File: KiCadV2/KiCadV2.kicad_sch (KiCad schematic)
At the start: 52 parts, among them J1 USB_C_Receptacle_PowerOnly_6P, J3 Screw_Terminal_01x02, J4 Screw_Terminal_01x02, U1 MT3608, U14 74LV08AT14-13, U16 NC7SZ157P6X, U17 MX3502S, U18 MX3502S, U2 74HC595, U26 MX3502S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

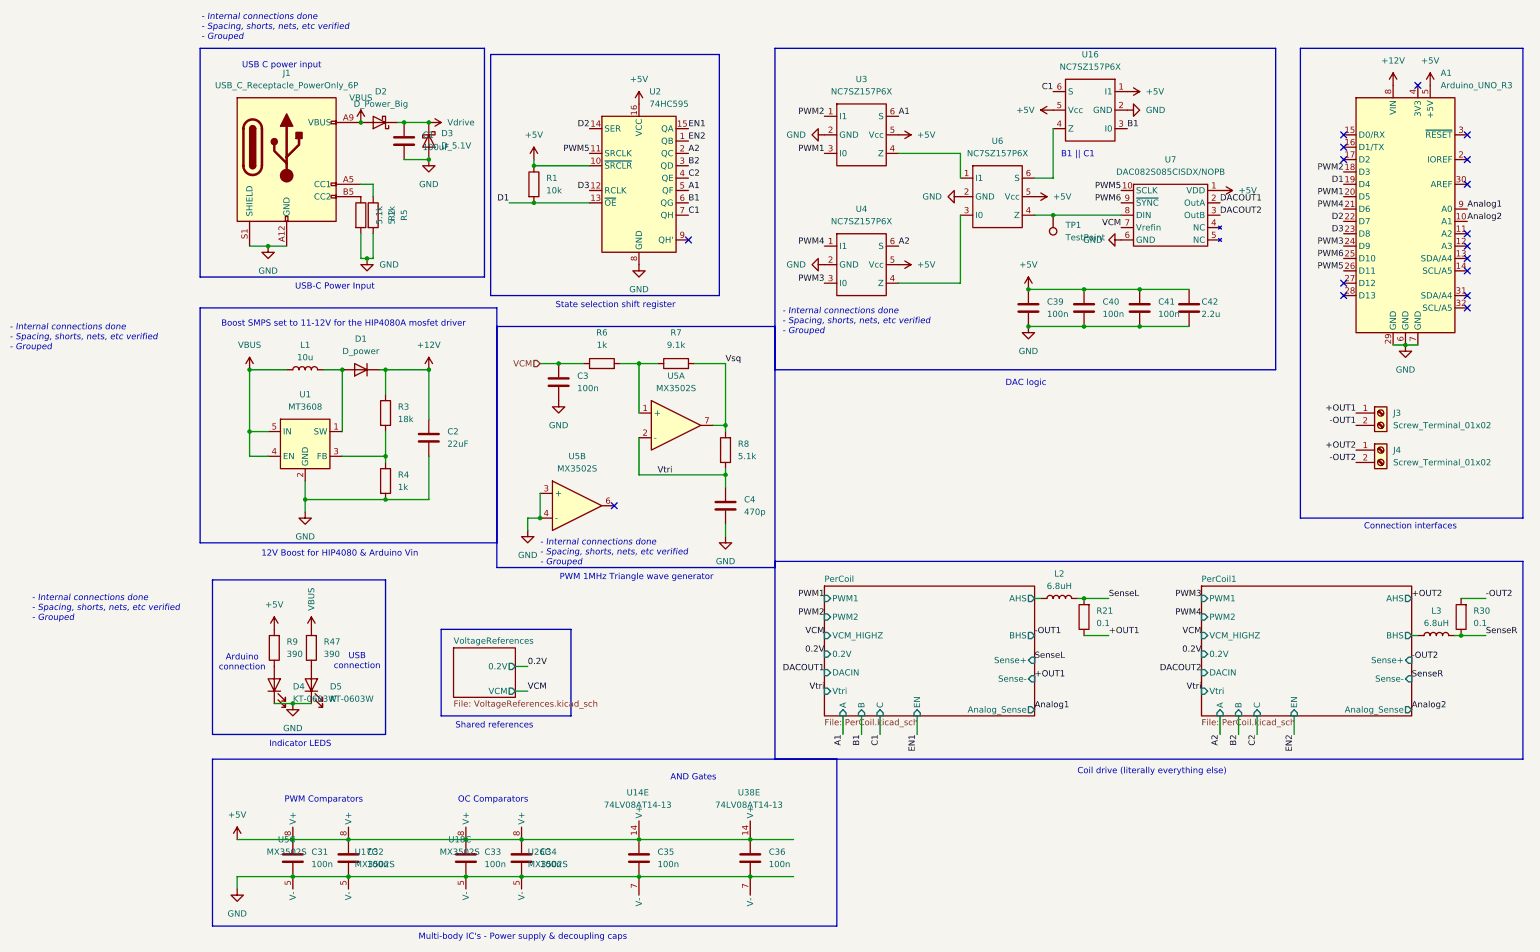
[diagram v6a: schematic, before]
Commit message: Fixed AND Gate pins, added extra DAC logic Mux
DAC logic mux not yet done on PCB
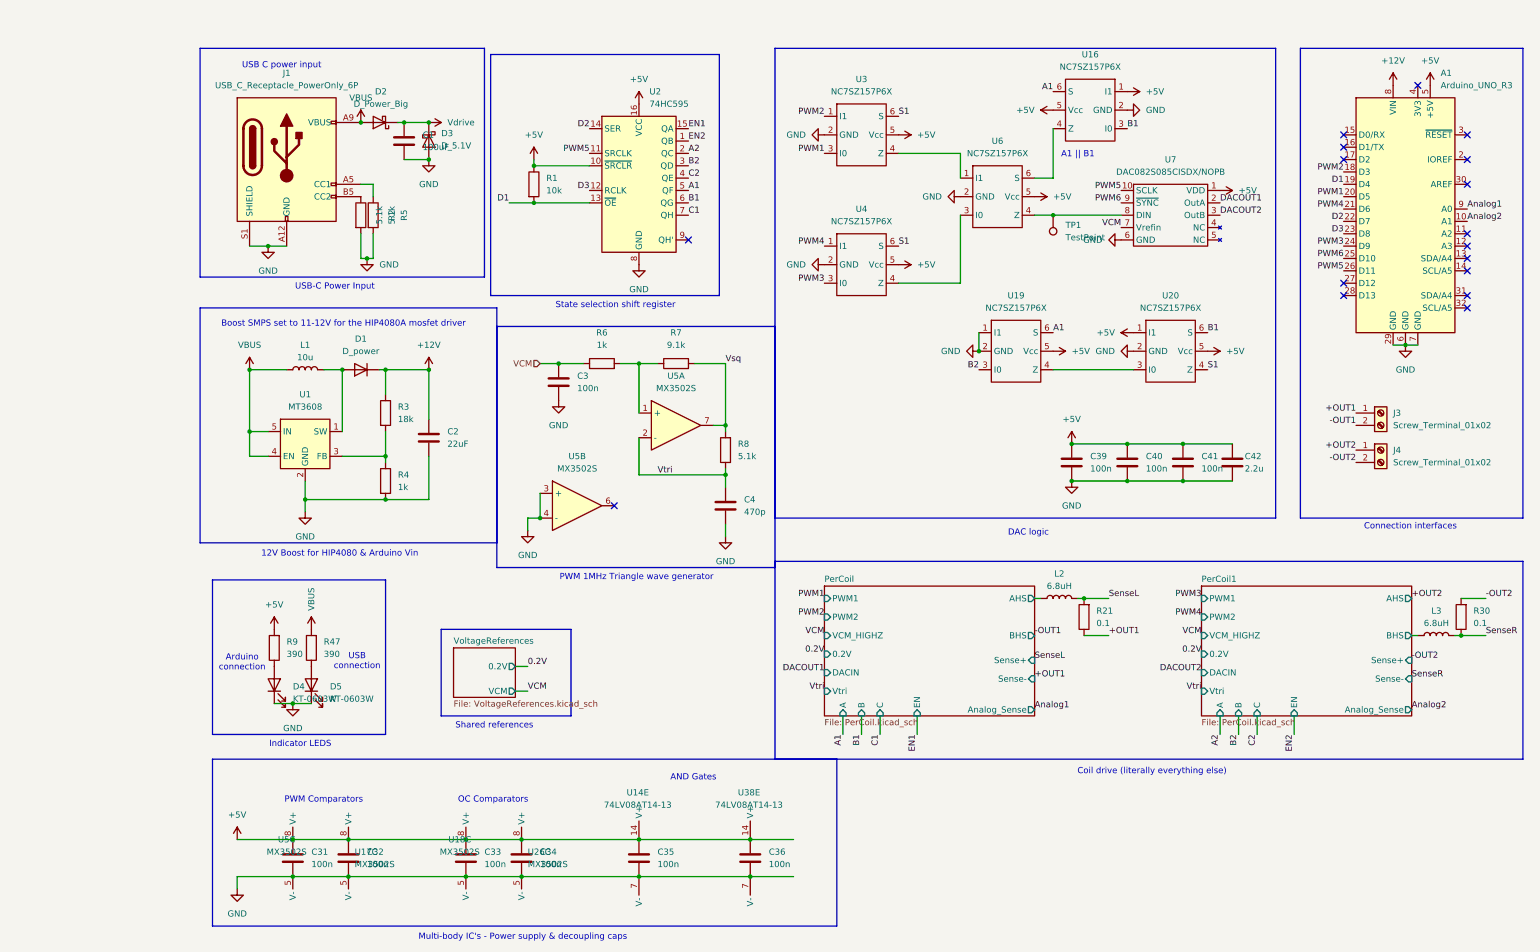
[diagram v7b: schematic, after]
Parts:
- added U19, U20: NC7SZ157P6X, Package_TO_SOT_SMD:SOT-363_SC-70-6, symbol 74xx:NC7SZ157P6X
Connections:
- net +5V: now also U19.5 (Vcc), U20.1 (I1), U20.5 (Vcc)
- net A1: now also U16.6 (S), U19.6 (S); no longer U3.6 (S)
- net A2: no longer U4.6 (S)
- net B1: now also U20.6 (S)
- net B2: now also U19.3 (I0)
- net C1: no longer U16.6 (S)
- net GND: now also U19.1 (I1), U19.2 (GND), U20.2 (GND)
- new net: U19.4 (Z), U20.3 (I0)
- new net S1: U20.4 (Z), U3.6 (S), U4.6 (S)
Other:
- note added: "A1 || B1"
- note removed: "- Internal connections done - Spacing, shorts, nets, etc verified - Grouped"
- note removed: "B1 || C1"
- moved on the sheet: C39, C40, C41, C42
